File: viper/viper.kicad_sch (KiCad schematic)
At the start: 127 parts, among them SW1 SW_Push, SW10 SW_Push, SW11 SW_Push, SW12 SW_Push, SW13 SW_Push, SW14 SW_Push, SW14_1 SW_Push, SW15 SW_Push, SW16 SW_Push, SW17 SW_Push, SW18 SW_Push, SW19 SW_Push, SW2 SW_Push, SW20 SW_Push, SW21 SW_Push, SW22 SW_Push, SW23 SW_Push, SW24 SW_Push, SW25 SW_Push, SW26 SW_Push, SW27 SW_Push, SW28 SW_Push, SW28_1 SW_Push, SW29 SW_Push, SW3 SW_Push, SW30 SW_Push, SW31 SW_Push, SW32 SW_Push, SW33 SW_Push, SW34 SW_Push, SW35 SW_Push, SW36 SW_Push, SW37 SW_Push, SW38 SW_Push, SW39 SW_Push, SW4 SW_Push, SW40 SW_Push, SW41 SW_Push, SW41_1 SW_Push, SW42 SW_Push, SW43 SW_Push, SW43_1 SW_Push, SW44 SW_Push, SW45 SW_Push, SW46 SW_Push, SW47 SW_Push, SW48 SW_Push, SW49 SW_Push, SW5 SW_Push, SW50 SW_Push, SW51 SW_Push, SW52 SW_Push, SW53 SW_Push, SW54 SW_Push, SW55 SW_Push, SW55_1 SW_Push, SW56 SW_Push, SW57 SW_Push, SW58 SW_Push, SW59 SW_Push, SW6 SW_Push, SW60 SW_Push, SW61 SW_Push, SW7 SW_Push, SW8 SW_Push, SW9 SW_Push

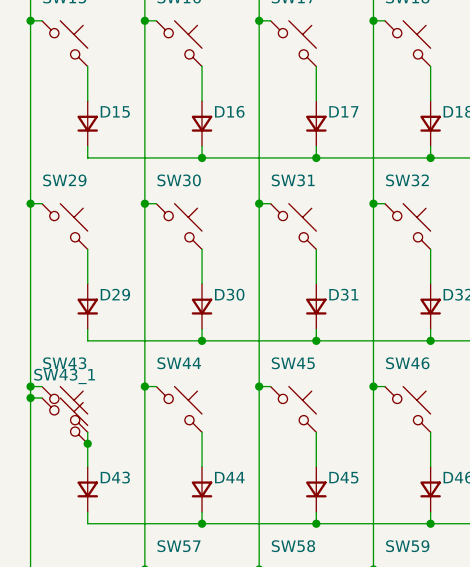
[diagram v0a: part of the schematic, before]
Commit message: Add updated export with stepped caps
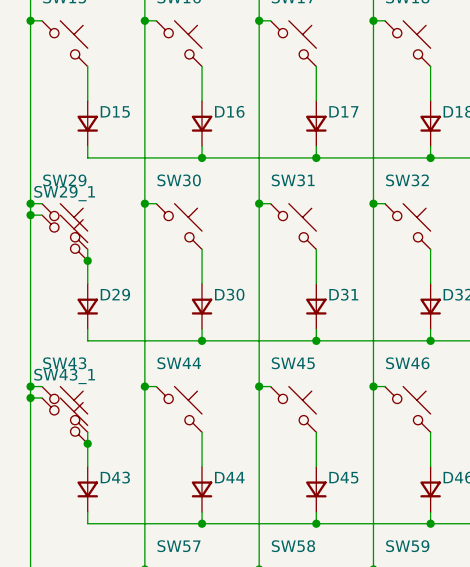
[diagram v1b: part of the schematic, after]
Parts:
- added SW29_1: SW_Push, Switch_Keyboard_Cherry_MX:SW_Cherry_MX_PCB_1.00u, symbol Switch:SW_Push_45deg
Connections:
- net COL0: now also SW29_1.1
- net at D29.2 (A), SW29.2: now also SW29_1.2

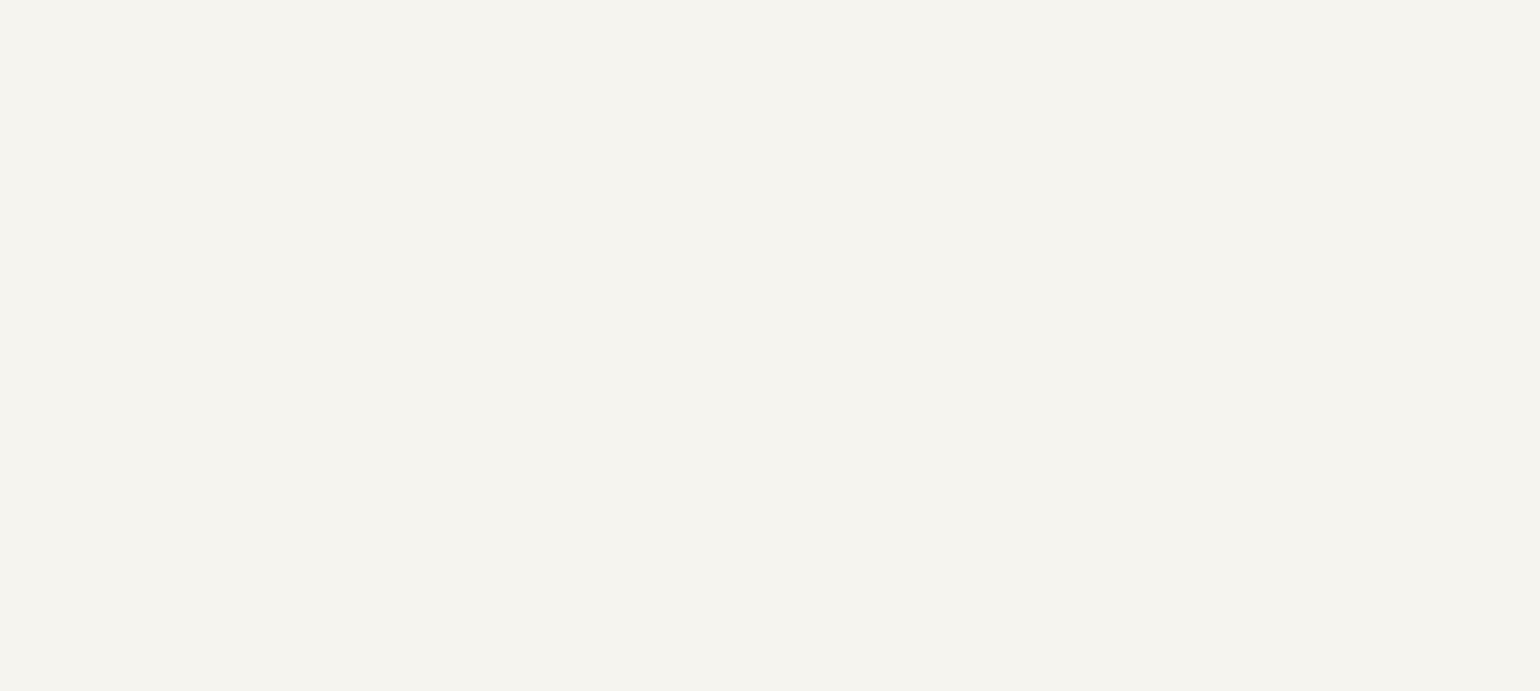
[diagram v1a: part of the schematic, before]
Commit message: kle2netlist with layout & netlist xml
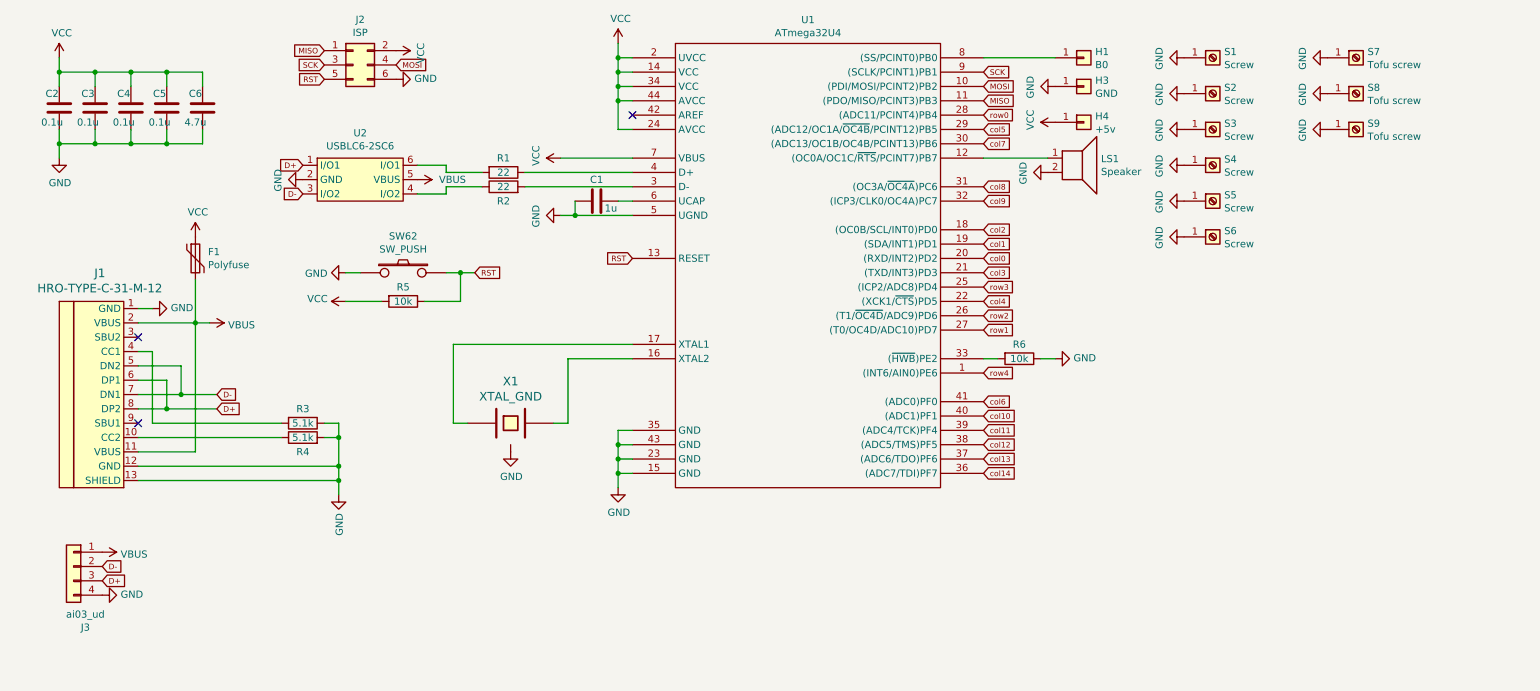
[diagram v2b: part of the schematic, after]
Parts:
- added C1: 1u, Keeb_components:C_0805, symbol Device:C
- added C2, C3, C4, C5: 0.1u, Keeb_components:C_0805, symbol Device:C
- added C6: 4.7u, Keeb_components:C_0805, symbol Device:C
- added F1: Polyfuse, Keeb_components:R_0805, symbol Device:Polyfuse
- added H1: B0, footprints:free_pin, symbol Connector_Generic:Conn_01x01
- added H3: GND, footprints:free_pin, symbol Connector_Generic:Conn_01x01
- added H4: +5v, footprints:free_pin, symbol Connector_Generic:Conn_01x01
- added J1: HRO-TYPE-C-31-M-12, Keeb_components:HRO-TYPE-C-31-M-12, symbol Type-C:HRO-TYPE-C-31-M-12
- added J2: ISP, Keeb_components:isp_standard, symbol Connector_Generic:Conn_02x03_Odd_Even
- added J3: ai03_ud, Keeb_components:JST_SH_SM04B-SRSS-TB_1x04-1MP_P1.00mm_Horizontal, symbol Connector_Generic:Conn_01x04
- added LS1: Speaker, Keeb_components:speaker_AST1109MLTRQ, symbol Device:Speaker
- added R1, R2: 22, Keeb_components:R_0805, symbol Device:R
- added R3, R4: 5.1k, Keeb_components:R_0805, symbol Device:R
- added R5, R6: 10k, Keeb_components:R_0805, symbol Device:R
- added S1, S2, S3, S6: Screw, footprints:5.5_5x2.5mm, symbol Connector:Screw_Terminal_01x01
- added S4, S5: Screw, footprints:10x5_7x2.5mm, symbol Connector:Screw_Terminal_01x01
- added S7, S8, S9: Tofu screw, footprints:5.5_5x2.5mm, symbol Connector:Screw_Terminal_01x01
- added SW62: SW_PUSH, Button_Switch_SMD:SW_SPST_TL3342, symbol keyboard_parts:SW_PUSH
- added U1: ATmega32U4, Keeb_components:ATMEGA32U4, symbol atmel:ATmega32U4
- added U2: USBLC6-2SC6, Keeb_components:USBLC6-2SC6, symbol keyboard_parts:USBLC6-2SC6
- added X1: XTAL_GND, Keeb_components:Resonator_SMD_muRata_CSTNExxV-3Pin-p1.2, symbol keyboard_parts:XTAL_GND
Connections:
- new net: LS1.1, U1.12 ((OC0A/OC1C/~{RTS}/PCINT7)PB7)
- new net: U1.16 (XTAL2), X1.2
- new net: U1.17 (XTAL1), X1.1
- new net: R2.2, U1.3 (D-)
- new net: R6.2, U1.33 ((~{HWB})PE2)
- new net: R1.1, U1.4 (D+)
- new net: C1.1, U1.6 (UCAP)
- new net: H1.1 (Pin_1), U1.8 ((SS/PCINT0)PB0)
- new net: R1.2, U2.6 (I/O1)
- new net: R2.1, U2.4 (I/O2)
- new net: J1.10 (CC2), R4.1
- new net: J1.4 (CC1), R3.2
- new net D+: J1.6 (DP1), J1.8 (DP2), J3.3 (Pin_3), U2.1 (I/O1)
- new net D-: J1.5 (DN2), J1.7 (DN1), J3.2 (Pin_2), U2.3 (I/O2)
- new net GND: C1.2, C2.1, C3.1, C4.1, C5.1, C6.1, H3.1 (Pin_1), J1.1 (GND), J1.12 (GND), J1.13 (SHIELD), J2.6 (Pin_6), J3.4 (Pin_4), LS1.2, R3.1, R4.2, R6.1, S1.1 (Pin_1), S2.1 (Pin_1), S3.1 (Pin_1), S4.1 (Pin_1), S5.1 (Pin_1), S6.1 (Pin_1), S7.1 (Pin_1), S8.1 (Pin_1), S9.1 (Pin_1), SW62.1, U1.15 (GND), U1.23 (GND), U1.35 (GND), U1.43 (GND), U1.5 (UGND), U2.2 (GND), X1.3
- new net MISO: J2.1 (Pin_1), U1.11 ((PDO/MISO/PCINT3)PB3)
- new net MOSI: J2.4 (Pin_4), U1.10 ((PDI/MOSI/PCINT2)PB2)
- new net RST: J2.5 (Pin_5), R5.1, SW62.2, U1.13 (RESET)
- new net SCK: J2.3 (Pin_3), U1.9 ((SCLK/PCINT1)PB1)
- new net VBUS: F1.2, J1.11 (VBUS), J1.2 (VBUS), J3.1 (Pin_1), U2.5 (VBUS)
- new net VCC: C2.2, C3.2, C4.2, C5.2, C6.2, F1.1, H4.1 (Pin_1), J2.2 (Pin_2), R5.2, U1.14 (VCC), U1.2 (UVCC), U1.24 (AVCC), U1.34 (VCC), U1.44 (AVCC), U1.7 (VBUS)
- new net col0: U1.20 ((RXD/INT2)PD2)
- new net col1: U1.19 ((SDA/INT1)PD1)
- new net col10: U1.40 ((ADC1)PF1)
- new net col11: U1.39 ((ADC4/TCK)PF4)
- new net col12: U1.38 ((ADC5/TMS)PF5)
- new net col13: U1.37 ((ADC6/TDO)PF6)
- new net col14: U1.36 ((ADC7/TDI)PF7)
- new net col2: U1.18 ((OC0B/SCL/INT0)PD0)
- new net col3: U1.21 ((TXD/INT3)PD3)
- new net col4: U1.22 ((XCK1/~{CTS})PD5)
- new net col5: U1.29 ((ADC12/OC1A/~{OC4B}/PCINT12)PB5)
- new net col6: U1.41 ((ADC0)PF0)
- new net col7: U1.30 ((ADC13/OC1B/OC4B/PCINT13)PB6)
- new net col8: U1.31 ((OC3A/~{OC4A})PC6)
- new net col9: U1.32 ((ICP3/CLK0/OC4A)PC7)
- new net row0: U1.28 ((ADC11/PCINT4)PB4)
- new net row1: U1.27 ((T0/OC4D/ADC10)PD7)
- new net row2: U1.26 ((T1/~{OC4D}/ADC9)PD6)
- new net row3: U1.25 ((ICP2/ADC8)PD4)
- new net row4: U1.1 ((INT6/AIN0)PE6)
- no-connect marks 0 -> 3

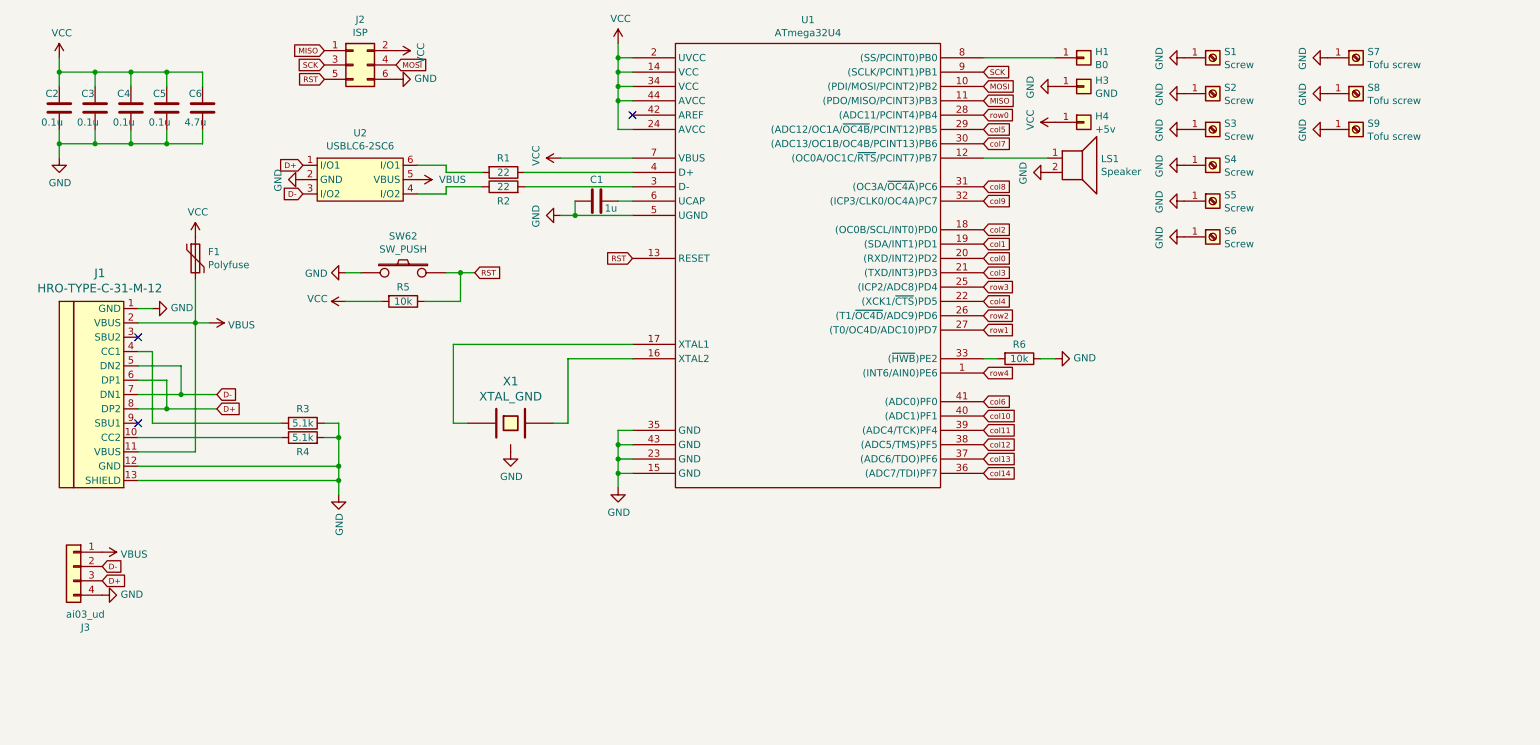
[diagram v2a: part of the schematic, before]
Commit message: Updated kle layout
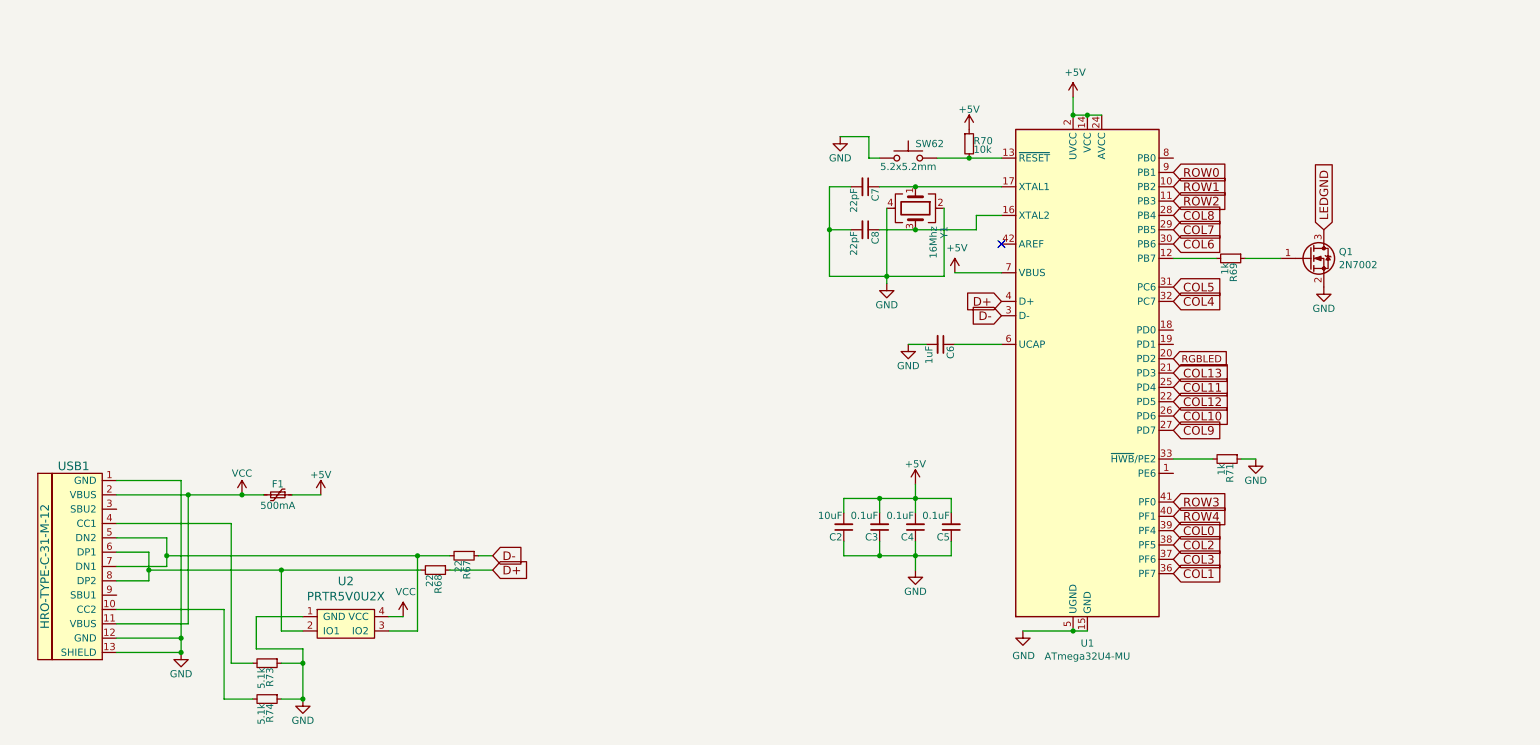
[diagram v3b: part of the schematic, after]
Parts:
- removed C1: 1u, Keeb_components:C_0805, symbol Device:C
- removed C2, C3, C4, C5: 0.1u, Keeb_components:C_0805, symbol Device:C
- removed C6: 4.7u, Keeb_components:C_0805, symbol Device:C
- removed F1: Polyfuse, Keeb_components:R_0805, symbol Device:Polyfuse
- removed H1: B0, footprints:free_pin, symbol Connector_Generic:Conn_01x01
- removed H3: GND, footprints:free_pin, symbol Connector_Generic:Conn_01x01
- removed H4: +5v, footprints:free_pin, symbol Connector_Generic:Conn_01x01
- removed J1: HRO-TYPE-C-31-M-12, Keeb_components:HRO-TYPE-C-31-M-12, symbol Type-C:HRO-TYPE-C-31-M-12
- removed J2: ISP, Keeb_components:isp_standard, symbol Connector_Generic:Conn_02x03_Odd_Even
- removed J3: ai03_ud, Keeb_components:JST_SH_SM04B-SRSS-TB_1x04-1MP_P1.00mm_Horizontal, symbol Connector_Generic:Conn_01x04
- removed LS1: Speaker, Keeb_components:speaker_AST1109MLTRQ, symbol Device:Speaker
- removed R1, R2: 22, Keeb_components:R_0805, symbol Device:R
- removed R3, R4: 5.1k, Keeb_components:R_0805, symbol Device:R
- removed R5, R6: 10k, Keeb_components:R_0805, symbol Device:R
- removed S1, S2, S3, S6: Screw, footprints:5.5_5x2.5mm, symbol Connector:Screw_Terminal_01x01
- removed S4, S5: Screw, footprints:10x5_7x2.5mm, symbol Connector:Screw_Terminal_01x01
- removed S7, S8, S9: Tofu screw, footprints:5.5_5x2.5mm, symbol Connector:Screw_Terminal_01x01
- removed SW62: SW_PUSH, Button_Switch_SMD:SW_SPST_TL3342, symbol keyboard_parts:SW_PUSH
- removed U1: ATmega32U4, Keeb_components:ATMEGA32U4, symbol atmel:ATmega32U4
- removed U2: USBLC6-2SC6, Keeb_components:USBLC6-2SC6, symbol keyboard_parts:USBLC6-2SC6
- removed X1: XTAL_GND, Keeb_components:Resonator_SMD_muRata_CSTNExxV-3Pin-p1.2, symbol keyboard_parts:XTAL_GND
- added C2: 10uF, Capacitors_SMD:C_0603, symbol Device:C_Small
- added C3, C4, C5: 0.1uF, Capacitors_SMD:C_0603, symbol Device:C_Small
- added C6: 1uF, Capacitors_SMD:C_0603, symbol Device:C_Small
- added C7, C8: 22pF, Capacitors_SMD:C_0603, symbol Device:C_Small
- added F1: 500mA, Fuse_Holders_and_Fuses:Fuse_SMD1206_Reflow, symbol Device:Polyfuse_Small
- added Q1: 2N7002, TO_SOT_Packages_SMD:SOT-23, symbol Transistor_FET:2N7002
- added R67, R68: 22, Resistors_SMD:R_0805, symbol Device:R_Small
- added R69, R71: 1k, Resistors_SMD:R_0805, symbol Device:R_Small
- added R70: 10k, Resistors_SMD:R_0805, symbol Device:R_Small
- added R73, R74: 5.1k, Resistors_SMD:R_0805, symbol Device:R_Small
- added SW62: 5.2x5.2mm, Molex-0548190589:SKQG-1155865, symbol Voyager60-rescue:SW_Push
- added U1: ATmega32U4-MU, Housings_DFN_QFN:QFN-44-1EP_7x7mm_Pitch0.5mm, symbol Voyager60-rescue:ATmega32U4-MU-MCU_Microchip_ATmega
- added U2: PRTR5V0U2X, locallib:SOT143B, symbol ai03-locallib:PRTR5V0U2X
- added USB1: HRO-TYPE-C-31-M-12, Type-C:HRO-TYPE-C-31-M-12-Assembly, symbol Type-C:HRO-TYPE-C-31-M-12
- added Y1: 16Mhz, Crystals:Crystal_SMD_3225-4pin_3.2x2.5mm, symbol Device:Crystal_GND24
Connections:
- net COL0: now also U1.39 (PF4)
- net COL1: now also U1.36 (PF7)
- net COL10: now also U1.26 (PD6)
- net COL11: now also U1.25 (PD4)
- net COL12: now also U1.22 (PD5)
- net COL13: now also U1.21 (PD3)
- net COL2: now also U1.38 (PF5)
- net COL3: now also U1.37 (PF6)
- net COL4: now also U1.32 (PC7)
- net COL5: now also U1.31 (PC6)
- net COL6: now also U1.30 (PB6)
- net COL7: now also U1.29 (PB5)
- net COL8: now also U1.28 (PB4)
- net COL9: now also U1.27 (PD7)
- net D+: now also R68.1, U1.4 (D+)
- net D-: now also R67.1, U1.3 (D-)
- net GND: now also C2.1, C3.1, C4.1, C5.1, C6.2, C7.2, C8.2, Q1.2 (S), R71.1, R73.1, R74.1, SW62.1, U1.15 (GND), U1.23 (GND), U1.35 (GND), U1.43 (GND), U1.45 (GND), U1.5 (UGND), U2.1 (GND), USB1.1 (GND), USB1.12 (GND), USB1.13 (SHIELD), Y1.2, Y1.4
- net ROW0: now also U1.9 (PB1)
- net ROW1: now also U1.10 (PB2)
- net ROW2: now also U1.11 (PB3)
- net ROW3: now also U1.41 (PF0)
- net ROW4: now also U1.40 (PF1)
- net VCC: now also F1.2, U2.4 (VCC), USB1.11 (VBUS), USB1.2 (VBUS)
- new net: C6.1, U1.6 (UCAP)
- new net: R70.2, SW62.2, U1.13 (~{RESET})
- new net: C7.1, U1.17 (XTAL1), Y1.1
- new net: C8.1, U1.16 (XTAL2), Y1.3
- new net: R71.2, U1.33 (~{HWB}/PE2)
- new net: Q1.1 (G), R69.1
- new net: R69.2, U1.12 (PB7)
- new net: R67.2, U2.3 (IO2), USB1.5 (DN2), USB1.7 (DN1)
- new net: R68.2, U2.2 (IO1), USB1.6 (DP1), USB1.8 (DP2)
- new net: R74.2, USB1.10 (CC2)
- new net: R73.2, USB1.4 (CC1)
- new net +5V: C2.2, C3.2, C4.2, C5.2, F1.1, R70.1, U1.14 (VCC), U1.2 (UVCC), U1.24 (AVCC), U1.34 (VCC), U1.44 (AVCC), U1.7 (VBUS)
- new net LEDGND: Q1.3 (D)
- new net RGBLED: U1.20 (PD2)
- no-connect marks 3 -> 1
